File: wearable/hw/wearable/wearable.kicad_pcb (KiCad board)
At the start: 4 copper layers, 81.5 x 38 mm, 102 parts, among them J2 Conn_02x05_Odd_Even, J3 USB-C Connector, SW1 SW_Toggle, U1 ADS1299IPAG, U3 BNO080, U4 nPM1300-QEXX, U5 LT3042xMSE, U6 TPS61040DBV, U7 BL54L15-453-000xxx, Y1 32.768kHz, Y2 32.768kHz

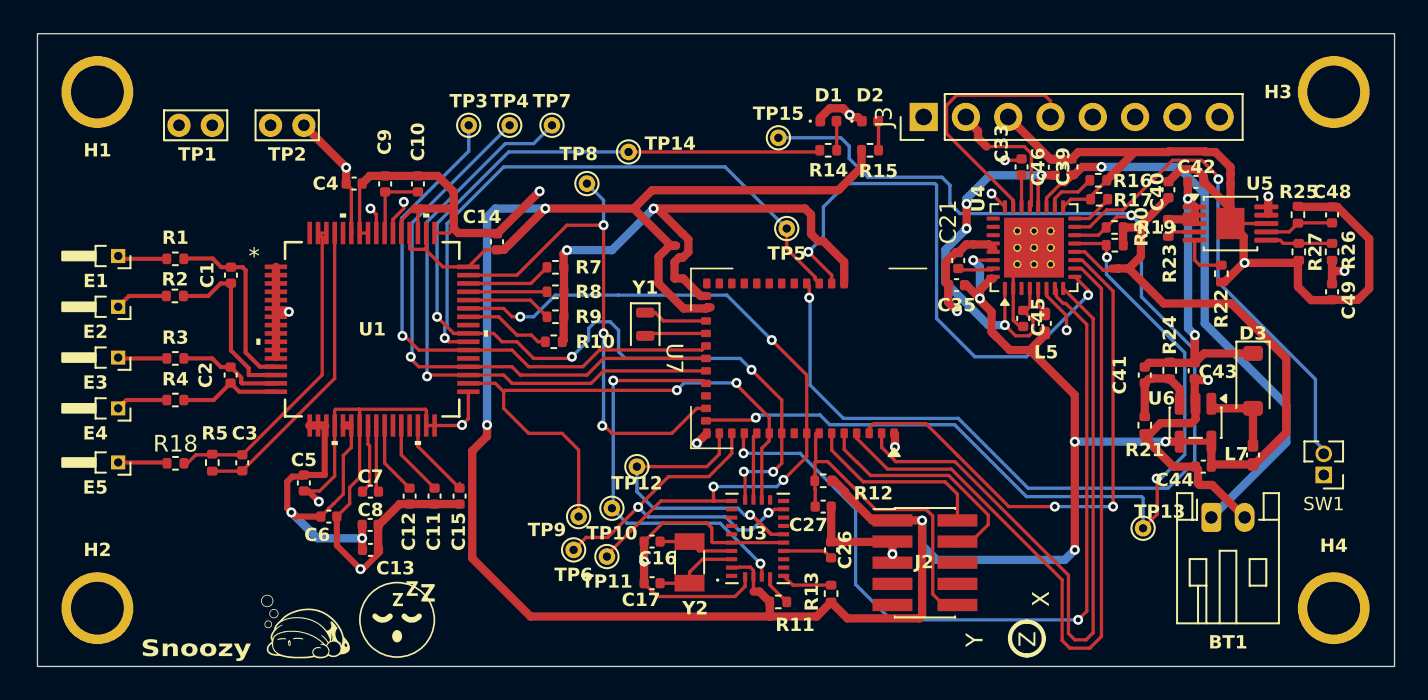
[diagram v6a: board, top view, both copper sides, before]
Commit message: Printout documents, reworked analog inputs
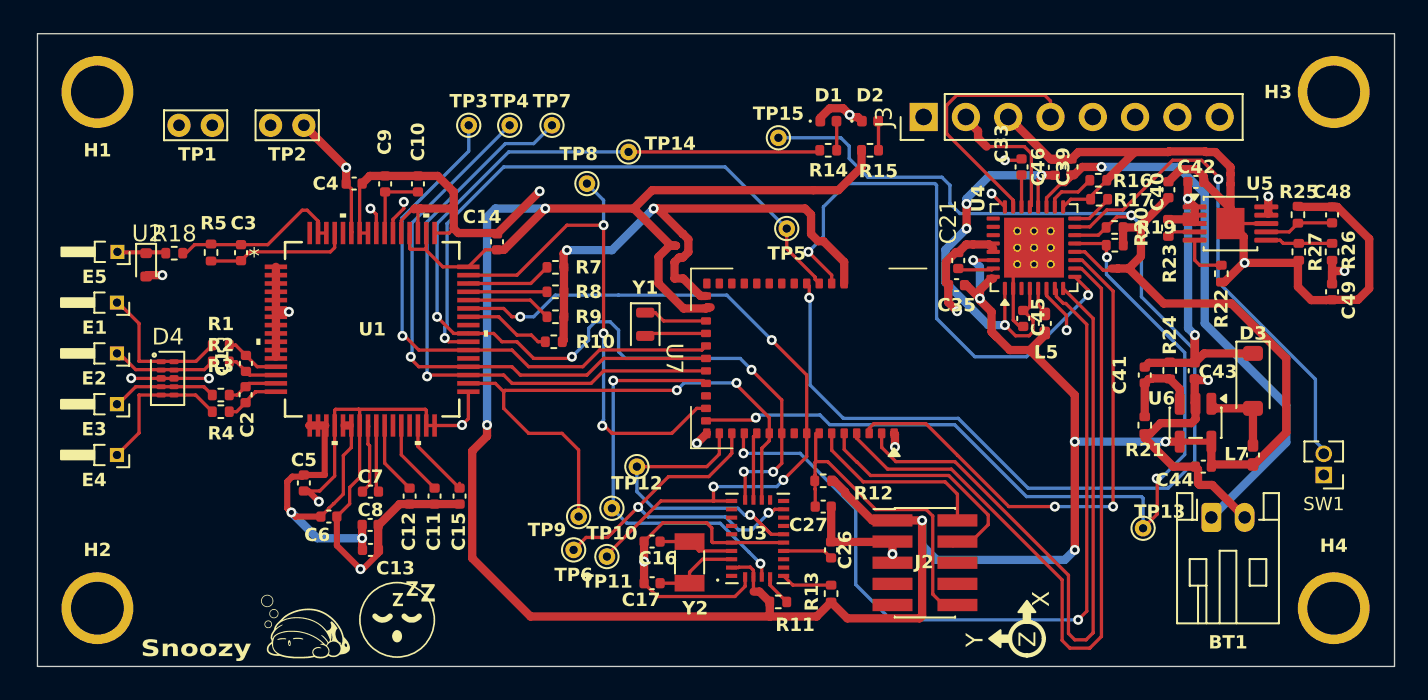
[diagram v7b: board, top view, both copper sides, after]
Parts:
- added D4: TPD4E05U06DQAR, PCM_Package_SON_AKL:USON-10_2.5x1.0mm_P0.5mm, F.Cu at (116.8, 103.2)
- added U2: TPD1E05U06DYA, Diode_SMD:D_SOD-523, F.Cu at (115.5, 96.4)
- moved E5 12.7 mm to (113.8, 95.6)
- moved R5 12.6 mm to (119.4, 95.6)
- moved C3 12.6 mm to (121.2, 95.7)
- moved R18 12.6 mm to (117.2, 95.7)
- moved R1 5.86 mm to (120.0, 101.2)
- moved C1 5.38 mm to (121.5, 102.3)
- moved R2 4.82 mm to (120.0, 102.2)
- moved R3 3.51 mm to (120.0, 104.2)
- moved R4 2.82 mm to (120.0, 105.2)
- moved E1 2.80 mm to (113.8, 98.7)
- moved E2 2.80 mm to (113.8, 101.7)
- moved E3 2.80 mm to (113.8, 104.8)
- moved E4 2.80 mm to (113.8, 107.8)
- moved C2 1.48 mm to (121.5, 104.2)
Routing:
- net Net-(U1-BIASINV): track 18.4 -> 8.60 mm
- net Net-(U1-BIASIN): track 20.0 -> 10.5 mm
- net Net-(U1-IN2P): track 10.8 -> 3.13 mm
- net Net-(U1-IN2N): track 11.1 -> 3.51 mm
- net Net-(D4-D1+): track 2.99 -> 8.95 mm
- net Net-(D4-D2-): track 3.13 -> 8.96 mm
- net AVSS: track 222.7 -> 228.4 mm, vias 17 -> 20
- net Net-(D4-D2+): track 2.94 -> 6.37 mm
- net Net-(D4-D1-): track 3.16 -> 6.35 mm
- net Net-(U1-IN1N): track 6.35 -> 3.23 mm
- net Net-(U1-IN1P): track 6.17 -> 3.42 mm

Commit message: Demo FW complete, PCB layout finalized (awaiting review from staff)
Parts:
- removed E2, E3, E4, E5: ~, Connector_PinHeader_1.00mm:PinHeader_1x01_P1.00mm_Horizontal
- removed TP13: TP, TestPoint:TestPoint_THTPad_D1.0mm_Drill0.5mm
- added TP16: TestPoint, TestPoint:TestPoint_THTPad_D1.0mm_Drill0.5mm, F.Cu at (175.4, 112.2)
- Elec_In: renamed from E1; footprint Connector_PinHeader_1.00mm:PinHeader_1x01_P1.00mm_Horizontal -> Connector_JST:JST_PH_S5B-PH-K_1x05_P2.00mm_Horizontal
- R12: value 10K -> 1K
- U4: footprint Package_DFN_QFN:QFN-32-1EP_5x5mm_P0.5mm_EP3.6x3.6mm_ThermalVias -> Unknown:QFN-32-1EP_5x5mm_P0.5mm_EP3.6x3.6mm_ThermalVias_D3x3.00mm
- moved Elec_In 1.07 mm to (112.8, 98.2), turned to -90 degrees
- turned R12 to 180 degrees
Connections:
- Elec_In pad 1: Net-(D4-D1+) -> VBIAS
- J3 pad 8: AVSS -> Net-(J3-Pin_8)
- R12 pad 1: RESET -> +3V3
- R12 pad 2: +3V3 -> RESET
- R18 pad 1: Net-(U2-I/O) -> VBIAS
- U2 pad 1: Net-(U2-I/O) -> VBIAS
- U4 pad 24: AVSS -> Net-(J3-Pin_8)
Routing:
- net Net-(J3-Pin_8): track 0.00 -> 30.3 mm
- net VBIAS: track 0.00 -> 4.62 mm
- net Net-(U2-I/O): track 2.88 -> 0.00 mm
- net Net-(D4-D1+): track 8.95 -> 7.52 mm
- net Net-(D4-D2-): track 8.96 -> 7.56 mm
- net AVSS: track 228.4 -> 229.6 mm, vias 20 -> 19
